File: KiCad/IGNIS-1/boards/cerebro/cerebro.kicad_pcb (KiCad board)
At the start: 2 copper layers, 19 parts, among them J1 LiPo_1S_in, J2 RBF_pin, J40 Backplane_2x10, Q1 MMBT3904, SW1 Main_SW, U10 ESP32-WROOM DevKit 38p

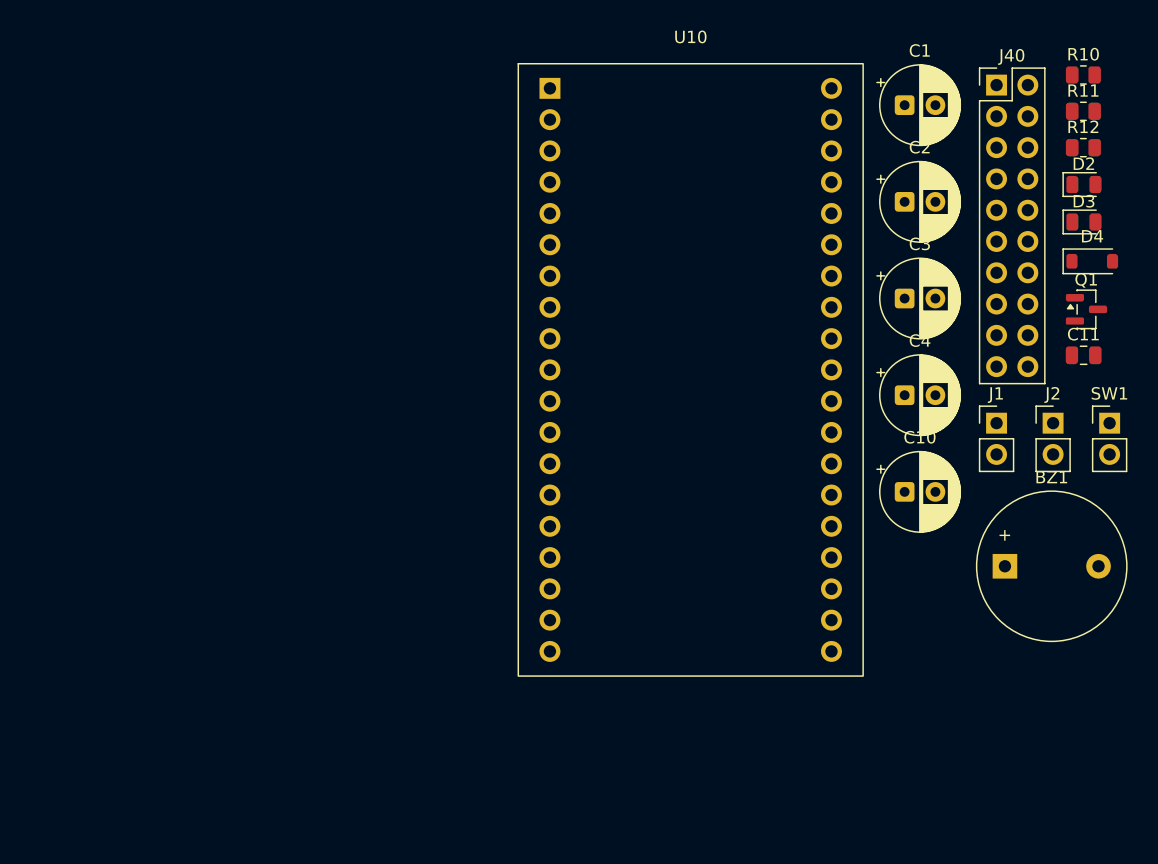
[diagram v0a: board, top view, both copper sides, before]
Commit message: PCB del MCU creado
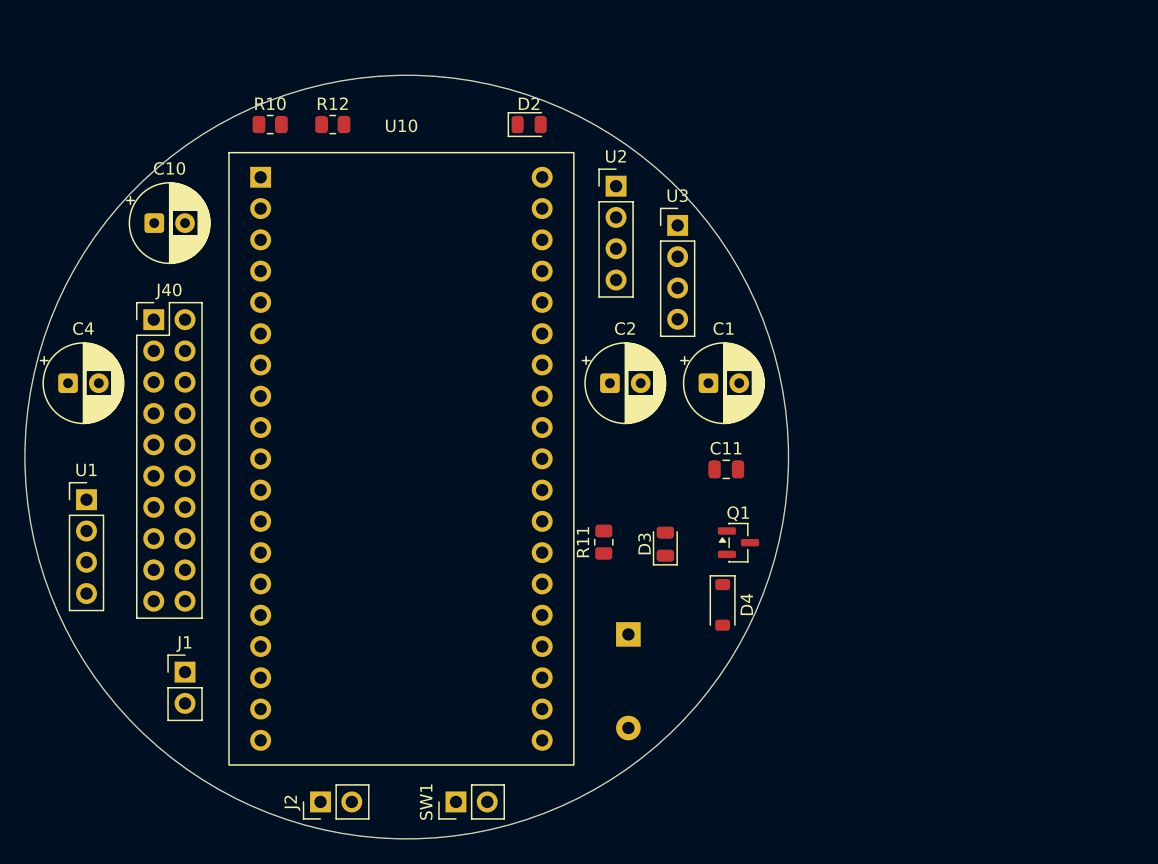
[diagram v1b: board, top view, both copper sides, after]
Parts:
- removed C3: 100uF, Capacitor_THT:CP_Radial_D6.3mm_P2.50mm
- added U1: Prot_1S_UVLO_OCP, Connector_PinHeader_2.54mm:PinHeader_1x04_P2.54mm_Vertical, F.Cu at (74.0, 103.5)
- added U2: BuckBoost_3V3, Connector_PinHeader_2.54mm:PinHeader_1x04_P2.54mm_Vertical, F.Cu at (117.0, 78.0)
- added U3: Boost_5V, Connector_PinHeader_2.54mm:PinHeader_1x04_P2.54mm_Vertical, F.Cu at (122.0, 81.2)
- BZ1: moved to B.Cu
- moved J40 71.0 mm to (79.5, 88.8)
- moved J1 68.9 mm to (82.0, 117.5)
- moved C4 67.9 mm to (72.5, 94.0)
- moved J2 67.0 mm to (93.0, 128.0), turned to 90 degrees
- moved R10 66.2 mm to (88.9, 73.0)
- moved C10 64.7 mm to (79.5, 81.0)
- moved SW1 61.3 mm to (104.0, 128.0), turned to 90 degrees
- moved R12 61.0 mm to (94.0, 73.0)
- moved R11 52.4 mm to (116.0, 106.9), turned to 90 degrees
- moved D2 45.3 mm to (109.9, 73.0)
- moved D3 42.9 mm to (121.0, 107.1), turned to 90 degrees
- moved D4 41.0 mm to (125.7, 112.0), turned to -90 degrees
- moved Q1 34.0 mm to (126.9, 107.0)
- moved BZ1 31.1 mm to (118.0, 114.4), turned to -90 degrees
- moved C11 30.5 mm to (126.0, 101.0)
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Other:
- board outline added: 62 x 62 mm

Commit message: Pines corregidos en ESP32
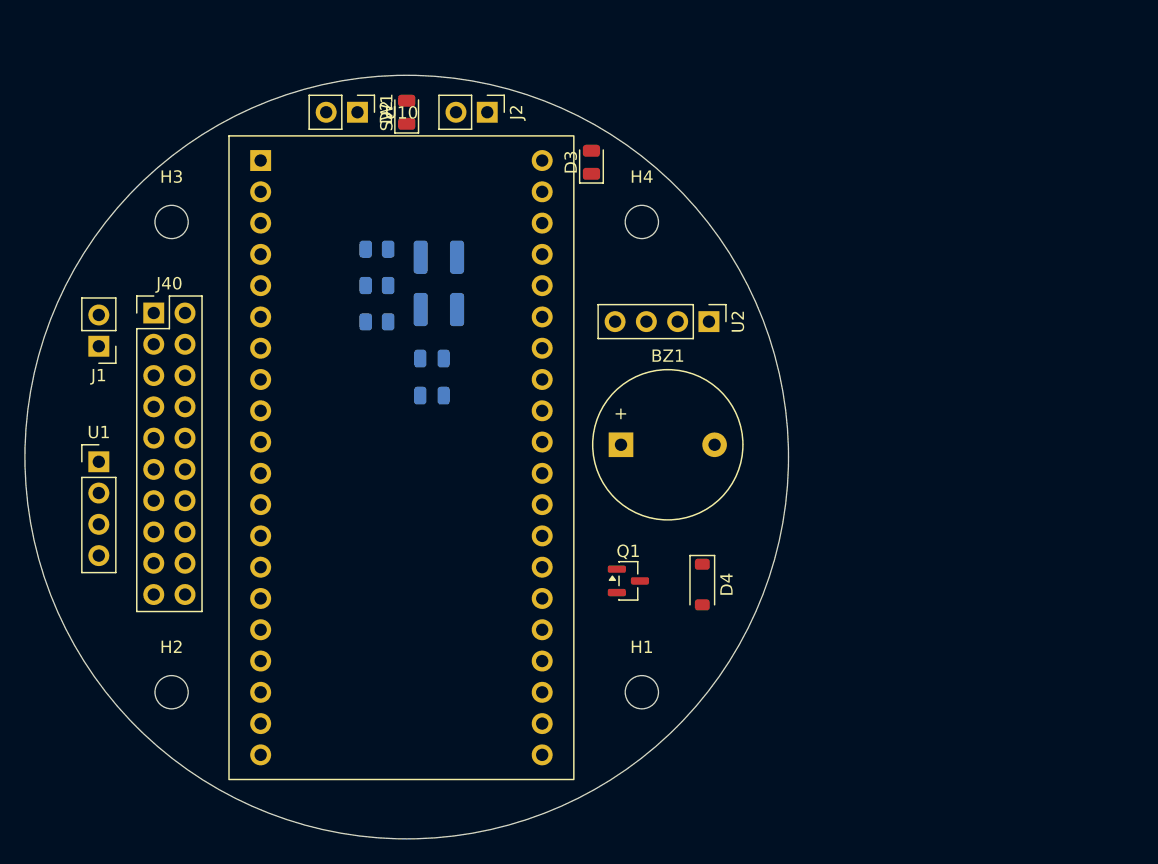
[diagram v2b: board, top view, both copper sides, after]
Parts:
- removed C4: 220uF, Capacitor_THT:CP_Radial_D6.3mm_P2.50mm
- removed U3: Boost_5V, Connector_PinHeader_2.54mm:PinHeader_1x04_P2.54mm_Vertical
- added H1: M2.5_hole, MountingHole:MountingHole_2.7mm_M2.5, F.Cu at (119.1, 119.1)
- added H2: M2.5_hole, MountingHole:MountingHole_2.7mm_M2.5, F.Cu at (80.9, 119.1)
- added H3: M2.5_hole, MountingHole:MountingHole_2.7mm_M2.5, F.Cu at (80.9, 80.9)
- added H4: M2.5_hole, MountingHole:MountingHole_2.7mm_M2.5, F.Cu at (119.1, 80.9)
- BZ1: moved to F.Cu
- C1: footprint Capacitor_THT:CP_Radial_D6.3mm_P2.50mm -> Capacitor_SMD:C_0805_2012Metric; moved to B.Cu
- C10, C2: footprint Capacitor_THT:CP_Radial_D6.3mm_P2.50mm -> Capacitor_SMD:C_1210_3225Metric; moved to B.Cu
- C11, R10, R11, R12: moved to B.Cu
- U10: value ESP32-WROOM DevKit 38p -> ESP32-WROOM-32E DevKit 40p; footprint IGNIS1:ESP32_DevKit_38p -> IGNIS1:ESP32_DevKit_40p
- moved J2 57.6 mm to (106.5, 72.0), turned to -90 degrees
- moved SW1 56.6 mm to (96.0, 72.0), turned to -90 degrees
- moved D3 31.6 mm to (115.0, 76.1)
- moved R11 27.8 mm to (97.6, 86.1), turned to 180 degrees
- moved J1 27.4 mm to (75.0, 91.0), turned to 180 degrees
- moved C11 24.6 mm to (102.0, 95.0), turned to 180 degrees
- moved C10 24.2 mm to (102.6, 88.0), turned to 180 degrees
- moved C1 22.5 mm to (102.0, 92.0), turned to 180 degrees
- moved C2 17.3 mm to (102.6, 83.8), turned to 180 degrees
- moved R12 16.4 mm to (97.6, 89.0), turned to 180 degrees
- moved BZ1 15.4 mm to (117.4, 99.0), turned to 0 degrees
- moved U2 13.3 mm to (124.5, 89.0), turned to -90 degrees
- moved R10 13.3 mm to (97.6, 83.1), turned to 180 degrees
- moved D2 9.99 mm to (100.0, 72.0), turned to 90 degrees
- moved Q1 9.46 mm to (118.0, 110.0)
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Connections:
- J40 pad 3: +5V -> unconnected-(J40-Pin_3-Pad3)
- U10 pad 10: SDA -> DIO0
- U10 pad 11: SCL -> MPU_INT
- U10 pad 12: MQ_AOUT -> LORA_RST
- U10 pad 16: unconnected-(U10-GPIO9-Pad16) -> +3V3
- U10 pad 17: unconnected-(U10-GPIO10-Pad17) -> +3V3
- U10 pad 21: MOSI -> GND
- U10 pad 22: unconnected-(U10-GPIO22-Pad22) -> MOSI
- U10 pad 26: GND -> unconnected-(U10-GPIO21-Pad26)
- U10 pad 27: MISO -> GND
- U10 pad 28: SCK -> MISO
- U10 pad 29: NSS_LORA -> SCK
- U10 pad 30: GPS_RX -> NSS_LORA
- U10 pad 31: GPS_TX -> GPS_RX
- U10 pad 32: /STATUS -> GPS_TX
- U10 pad 33: unconnected-(U10-GPIO0-Pad33) -> /STATUS
- U10 pad 37: unconnected-(U10-GPIO7-Pad37) -> GND
- U10 pad 38: unconnected-(U10-GPIO6-Pad38) -> GND
- U10 pad 6: LORA_RST -> MQ_AOUT
- U10 pad 7: MPU_INT -> SCL
- U10 pad 8: DIO0 -> SDA

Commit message: Schematic arreglado. Footprint del ESP32 ajustado.
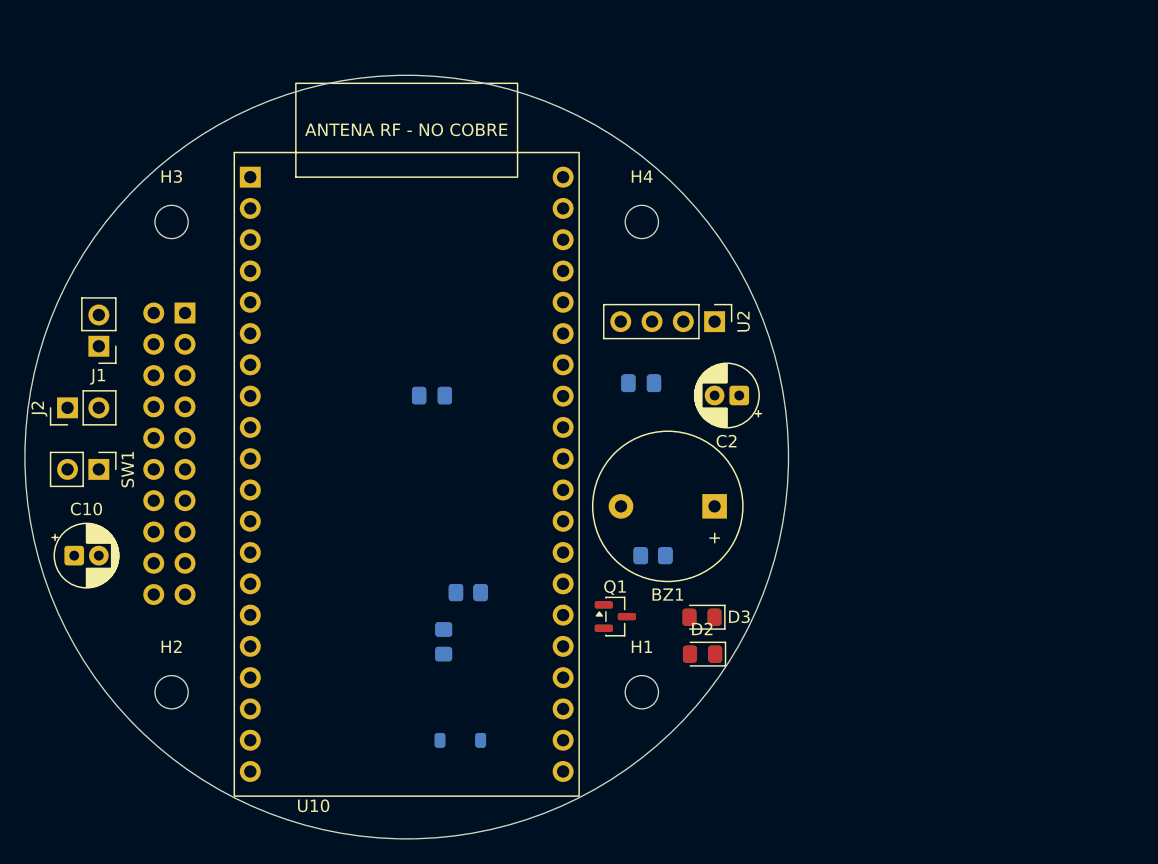
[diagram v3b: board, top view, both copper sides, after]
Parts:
- removed U1: Prot_1S_UVLO_OCP, Connector_PinHeader_2.54mm:PinHeader_1x04_P2.54mm_Vertical
- C1, C11: footprint Capacitor_SMD:C_0805_2012Metric -> Capacitor_SMD:C_0805_2012Metric_Pad1.18x1.45mm_HandSolder
- C10, C2: footprint Capacitor_SMD:C_1210_3225Metric -> Capacitor_THT:CP_Radial_D5.0mm_P2.00mm; moved to F.Cu
- D2, D3: footprint LED_SMD:LED_0805_2012Metric -> LED_SMD:LED_0805_2012Metric_Pad1.15x1.40mm_HandSolder
- D4, J40: moved to B.Cu
- R10, R11, R12: footprint Resistor_SMD:R_0805_2012Metric -> Resistor_SMD:R_0805_2012Metric_Pad1.20x1.40mm_HandSolder
- moved D2 50.1 mm to (124.0, 116.0), turned to 180 degrees
- moved J2 41.7 mm to (72.5, 96.0), turned to 90 degrees
- moved D3 38.0 mm to (124.0, 113.0), turned to 180 degrees
- moved SW1 35.8 mm to (75.0, 101.0)
- moved C10 35.7 mm to (73.0, 108.0), turned to 0 degrees
- moved R10 32.3 mm to (103.0, 115.0), turned to 90 degrees
- moved R11 31.4 mm to (120.0, 108.0), turned to 0 degrees
- moved C2 26.9 mm to (127.0, 95.0)
- moved D4 23.4 mm to (104.3, 123.0), turned to 0 degrees
- moved R12 23.2 mm to (105.0, 111.0), turned to 0 degrees
- moved C1 17.1 mm to (119.0, 94.0), turned to 0 degrees
- moved BZ1 9.10 mm to (125.0, 104.0), turned to 180 degrees
- moved Q1 3.09 mm to (116.9, 113.0)
- moved J40 2.54 mm to (82.0, 88.3), turned to 180 degrees
- moved U10 1.42 mm to (100.0, 101.4)
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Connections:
- J2 pad 1: /VSYS -> +BATT
